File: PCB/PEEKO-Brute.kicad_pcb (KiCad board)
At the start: 2 copper layers, 52.1 x 45.7 mm, 61 parts, among them J1 Rasberry PI Pico, J2 Conn_02x15_Odd_Even, J3 Conn_01x02_Pin, J4 Conn_01x02_Pin

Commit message: add fab bom and centroid exports
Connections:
- J2 pad 3: /TRIGGER -> unconnected-(J2-Pin_3-Pad3)

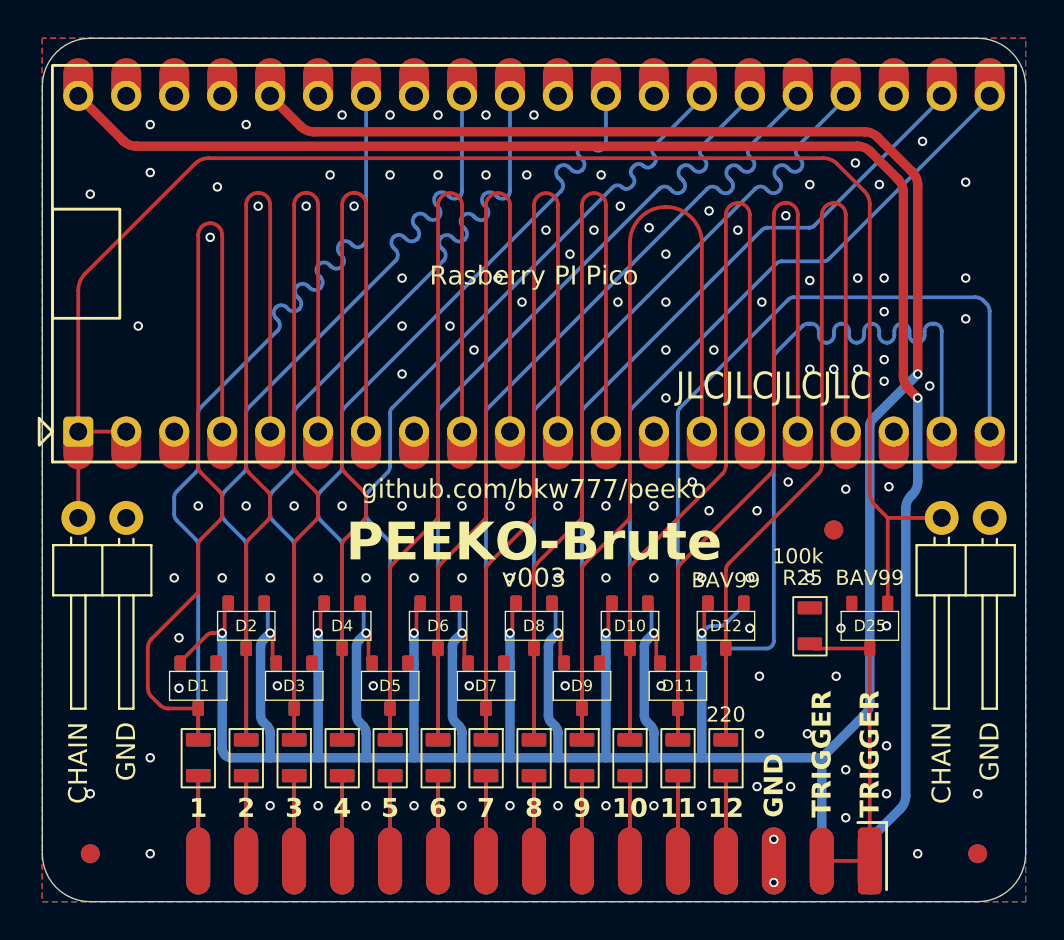
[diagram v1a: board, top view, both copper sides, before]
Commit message: switch to schottkys on brute
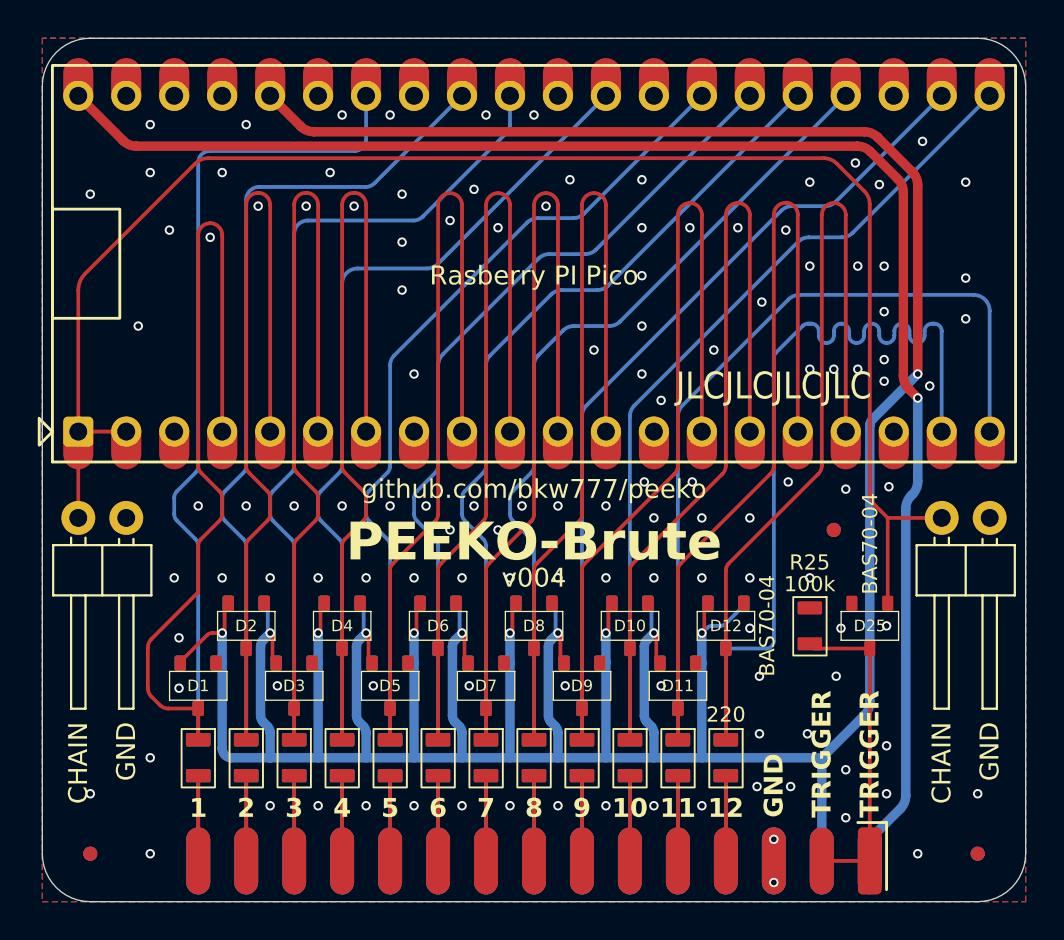
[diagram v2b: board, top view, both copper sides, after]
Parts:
- removed the REF** at (169.5, 126.0) (x2)
- removed the REF** at (122.5, 126.0) (x2)
- removed the REF** at (161.9, 108.8) (x2)
- added REF**: Fiducial_1.5, 000_LOCAL:Fiducial_1.5, F.Cu at (122.5, 126.0)
- added REF**: Fiducial_1.5, 000_LOCAL:Fiducial_1.5, F.Cu at (161.9, 108.8)
- added REF**: Fiducial_1.5, 000_LOCAL:Fiducial_1.5, F.Cu at (169.5, 126.0)
- added REF**: Fiducial_1.5, 000_LOCAL:Fiducial_1.5, B.Cu at (122.5, 126.0)
- added REF**: Fiducial_1.5, 000_LOCAL:Fiducial_1.5, B.Cu at (161.9, 108.8)
- added REF**: Fiducial_1.5, 000_LOCAL:Fiducial_1.5, B.Cu at (169.5, 126.0)
- D1, D10, D11, D12, D13, D14, D15, D16, D17, D18, D19, D2, D20, D21, D22, D23, D24, D25, D3, D4, D5, D6, D7, D8, D9: value BAV99 -> BAS70-04
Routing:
- net /_CH12: track 43.8 -> 43.0 mm
- net GND: vias 127 -> 125

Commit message: make brute the same dimensions and port placement as regular peeko, use same housing for both
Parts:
- N1: value PEEKO-Brute Housing -> PEEKO Housing; footprint 000_LOCAL:PEEKO-Brute_housing -> 000_LOCAL:PEEKO_housing
- moved J3 8.89 mm to (161.3, 108.2), turned to 0 degrees
- moved REF** 7.31 mm to (168.9, 106.7) (x2)
- moved J4 6.84 mm to (130.8, 110.7), turned to 180 degrees
- moved D25 3.02 mm to (162.8, 116.8)
- moved R25 2.93 mm to (160.0, 116.8)
- moved REF** 2.54 mm to (122.5, 123.4) (x2)
- moved REF** 2.54 mm to (169.5, 123.4) (x2)
- moved J2 2.41 mm to (146.0, 126.1)
- moved N1 1.27 mm to (146.0, 104.4)
- moved R1 0.57 mm to (128.2, 120.3)
- moved R10 0.57 mm to (151.1, 120.3)
- moved R11 0.57 mm to (153.6, 120.3)
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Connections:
- J2 pad 3: unconnected-(J2-Pin_3-Pad3) -> /TRIGGER
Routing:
- net /CHAIN: track 85.1 -> 93.4 mm
- net +3V3: track 215.5 -> 210.1 mm
- net /TRIGGER: track 17.1 -> 12.2 mm
- net +5V: track 82.5 -> 80.2 mm
- net /CH9: track 4.51 -> 2.67 mm
- net /CH8: track 4.51 -> 2.67 mm
- net /CH7: track 4.51 -> 2.67 mm
- net /CH6: track 4.51 -> 2.67 mm
- net /CH5: track 4.51 -> 2.67 mm
- net /CH4: track 4.51 -> 2.67 mm
- net /CH3: track 4.51 -> 2.67 mm
- net /CH23: track 4.51 -> 2.67 mm
- net /CH22: track 4.51 -> 2.67 mm
- net /CH21: track 4.51 -> 2.67 mm
- net /CH20: track 4.51 -> 2.67 mm
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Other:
- board size 52.1 x 45.7 mm -> 52.1 x 43.2 mm
- board text added: "TRIG"
- board text added: "trace lengths 38.16 + 4.58 = 42.74 41.34 + 1.40 = 42.74"
- board text removed: "TRIGGER"
- board text removed: "trace lengths 38.46 + 4.84 = 43.3 41.64 + 1.66 = 43.3"

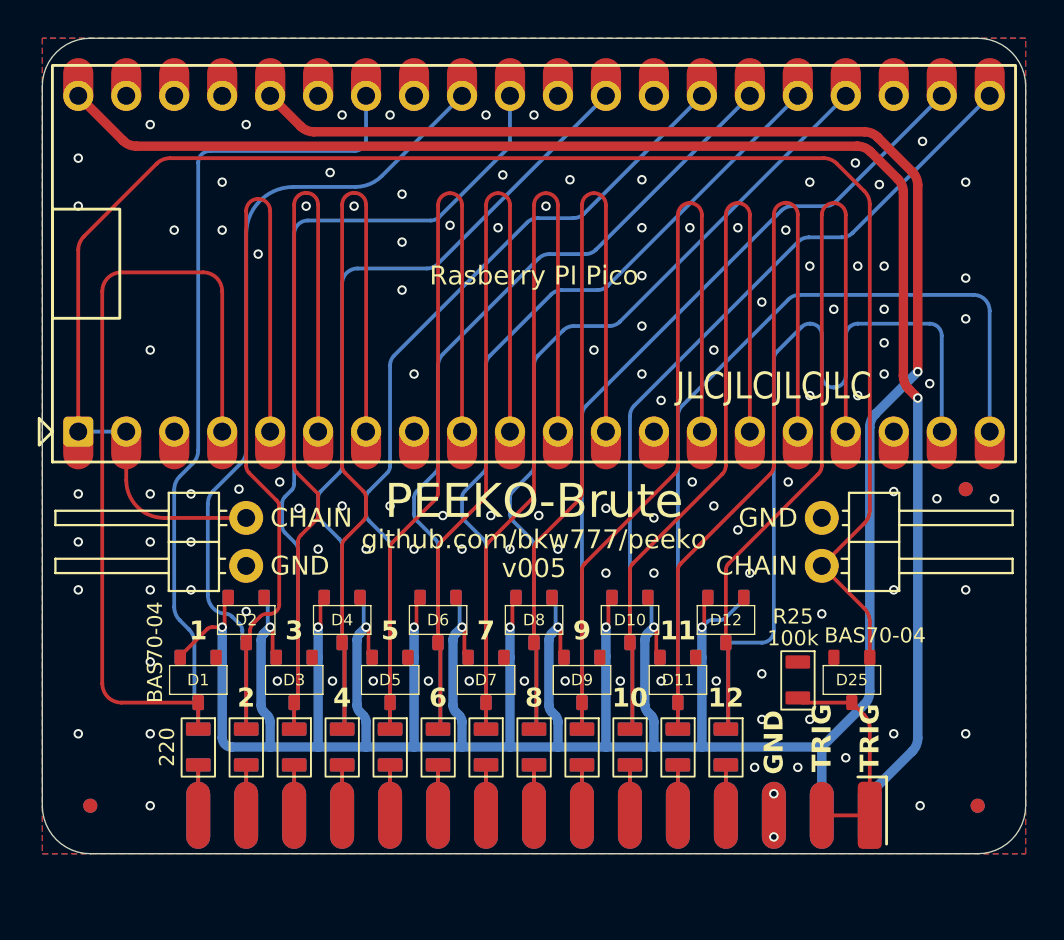
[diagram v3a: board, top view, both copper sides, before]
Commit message: make both boards have same chain pinout
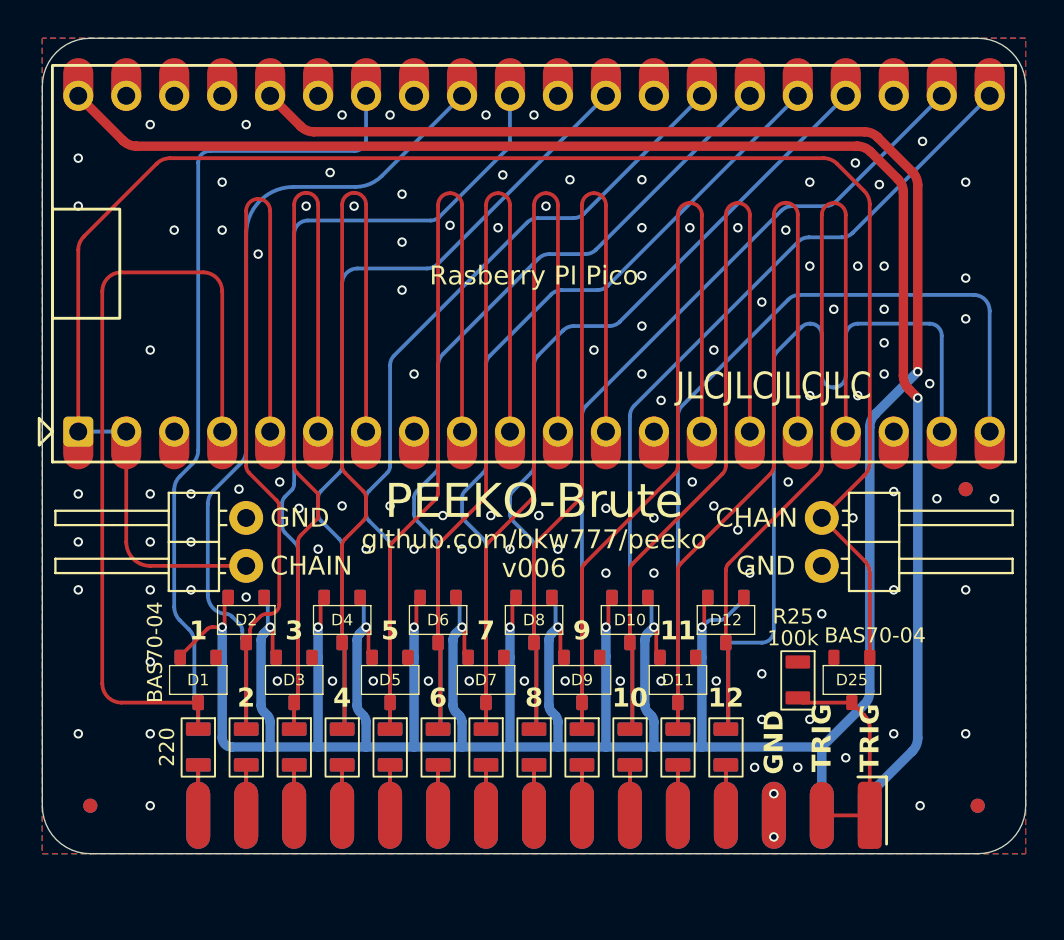
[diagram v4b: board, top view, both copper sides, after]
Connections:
- J3 pad 1: GND -> /CHAIN
- J3 pad 2: /CHAIN -> GND
- J4 pad 1: GND -> /CHAIN
- J4 pad 2: /CHAIN -> GND
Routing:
- net /CHAIN: track 93.4 -> 96.2 mm
- net GND: vias 118 -> 119
